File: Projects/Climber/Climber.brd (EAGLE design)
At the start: 160 x 100 mm, 3 parts, among them M1 VNH5019, M2 D36V6FX, U1 NRF52840-DONGLE

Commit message: New devices in Climber
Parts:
- added R1, R2: (no value), resistor:R0603
- added U$10: NET_CONN, NET_CONN:NET_CONN
- added U2: BSS138BKW, BSS138:SOT65P210X110-3N
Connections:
- net VOUT renamed M1_VOUT
- new net M1_CS: M1.CS
- new net M1_ENA/DIAGA: M1.ENA
- new net M1_ENB/DIAGB: M1.ENB
- new net M1_INA: M1.INA
- new net M1_INB: M1.INB
- new net M1_PWM: M1.PWM
- new net NEO_HV: R2.1, U2.3
- new net NEO_LV: R1.1, U2.2
- new net VDD_5V: R2.2
- net GND: now also U$10.1, U$10.2
- net VDD: now also M2.VOUT, R1.2, U1.OUT
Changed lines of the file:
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@@
 <layer number="111" name="LPC17xx" color="7" fill="1" visible="yes" active="yes"/>
 <layer number="112" name="tSilk" color="7" fill="1" visible="yes" active="yes"/>
+<layer number="113" name="FRNTTEKEN" color="7" fill="1" visible="yes" active="yes"/>
+<layer number="114" name="FRNTMAAT1" color="7" fill="1" visible="yes" active="yes"/>
+<layer number="115" name="FRNTMAAT2" color="7" fill="1" visible="yes" active="yes"/>
 <layer number="116" name="Patch_BOT" color="9" fill="4" visible="yes" active="yes"/>
+<layer number="117" name="BACKMAAT1" color="7" fill="1" visible="yes" active="yes"/>
+<layer number="118" name="BACKMAAT2" color="7" fill="1" visible="yes" active="yes"/>
+<layer number="119" name="KAP_TEKEN" color="7" fill="1" visible="yes" active="yes"/>
 <layer number="120" name="_Dimension" color="7" fill="1" visible="yes" active="yes"/>
 <layer number="121" name="_tsilk" color="6" fill="1" visible="yes" active="yes"/>
@@
 <layer number="127" name="_tValues" color="6" fill="1" visible="yes" active="yes"/>
 <layer number="128" name="_bValues" color="6" fill="1" visible="yes" active="yes"/>
+<layer number="130" name="SMDSTROOK" color="7" fill="1" visible="yes" active="yes"/>
 <layer number="131" name="tAdjust" color="7" fill="1" visible="yes" active="yes"/>
 <layer number="132" name="bAdjust" color="7" fill="1" visible="yes" active="yes"/>
@@
 <layer number="251" name="bxdocu" color="7" fill="1" visible="no" active="yes"/>
 <layer number="254" name="cooling" color="7" fill="1" visible="yes" active="yes"/>
+<layer number="255" name="Accent" color="7" fill="1" visible="yes" active="yes"/>
 </layers>
 <board>
@@
 <attribute name="VALUE" x="30.9626" y="59.69" size="1.27" layer="27" rot="R180"/>
 </element>
+<element name="U2" library="BSS138" package="SOT65P210X110-3N" value="BSS138BKW" x="-17.78" y="2.54" smashed="yes">
+<attribute name="MPN" value="BSS138BKW" x="-17.78" y="2.54" size="1.778" layer="27" display="off"/>
+<attribute name="NAME" x="-18.3642" y="3.8196" size="0.254" layer="25" ratio="10" rot="SR0"/>
+<attribute name="OC_FARNELL" value="2053836" x="-17.78" y="2.54" size="1.778" layer="27" display="off"/>
+<attribute name="OC_NEWARK" value="61T7488" x="-17.78" y="2.54" size="1.778" layer="27" display="off"/>
+<attribute name="PACKAGE" value="SOT-23-3" x="-17.78" y="2.54" size="1.778" layer="27" display="off"/>
+<attribute name="SUPPLIER" value="NXP" x="-17.78" y="2.54" size="1.778" layer="27" display="off"/>
+<attribute name="VALUE" x="-18.3642" y="1.043" size="0.254" layer="27" ratio="10" rot="SR0"/>
+</element>
+<element name="U$10" library="NET_CONN" package="NET_CONN" value="NET_CONN" x="-19.05" y="-1.27" smashed="yes"/>
+<element name="R1" library="resistor" package="R0603" value="" x="-17.78" y="-5.08" smashed="yes">
+<attribute name="NAME" x="-17.526" y="-3.937" size="0.381" layer="25" rot="R180"/>
+<attribute name="VALUE" x="-19.304" y="-6.223" size="0.381" layer="27"/>
+</element>
+<element name="R2" library="resistor" package="R0603" value="" x="-17.78" y="-8.89" smashed="yes">
+<attribute name="NAME" x="-17.526" y="-7.747" size="0.381" layer="25" rot="R180"/>
+<attribute name="VALUE" x="-19.304" y="-10.033" size="0.381" layer="27"/>
+</element>
 </elements>
 <signals>
 <signal name="VDD">
 <contactref element="M1" pad="VDD"/>
+<contactref element="M2" pad="VOUT"/>
+<contactref element="U1" pad="OUT"/>
+<contactref element="R1" pad="2"/>
+<wire x1="44.45" y1="83.82" x2="57.15" y2="86.36" width="0" layer="19" extent="1-1"/>
+<wire x1="5.0876" y1="57.15" x2="44.45" y2="83.82" width="0" layer="19" extent="1-1"/>
+<wire x1="-16.93" y1="-5.08" x2="5.0876" y2="57.15" width="0" layer="19" extent="1-1"/>
 </signal>
 <signal name="GND">
 <contactref element="M1" pad="GND@0"/>
 <contactref element="M1" pad="GND@1"/>
+<contactref element="U1" pad="G3"/>
+<contactref element="U1" pad="G1"/>
+<contactref element="U1" pad="G2"/>
+<contactref element="U$10" pad="1"/>
+<contactref element="U$10" pad="2"/>
 <contactref element="M2" pad="GND"/>
-<contactref element="U1" pad="G1"/>
-<contactref element="U1" pad="G3"/>
-<contactref element="U1" pad="G2"/>
 <wire x1="44.45" y1="86.36" x2="59.69" y2="86.36" width="0" layer="19" extent="1-1"/>
 <wire x1="44.45" y1="91.44" x2="44.45" y2="86.36" width="0" layer="19" extent="1-1"/>
-<wire x1="25.4076" y1="41.91" x2="44.45" y2="86.36" width="0" layer="19" extent="1-1"/>
-<wire x1="25.4076" y1="57.15" x2="25.4076" y2="41.91" width="0" layer="19" extent="1-1"/>
+<wire x1="25.4076" y1="57.15" x2="44.45" y2="86.36" width="0" layer="19" extent="1-1"/>
+<wire x1="25.4076" y1="41.91" x2="25.4076" y2="57.15" width="0" layer="19" extent="1-1"/>
 <wire x1="7.6276" y1="57.15" x2="25.4076" y2="57.15" width="0" layer="19" extent="1-1"/>
-</signal>
-<signal name="VOUT">
-<contactref element="M1" pad="VOUT"/>
+<wire x1="-17.55" y1="-1.27" x2="25.4076" y2="41.91" width="0" layer="19" extent="1-1"/>
+<wire x1="-18.669" y1="-1.27" x2="-17.55" y2="-1.27" width="0" layer="19" extent="1-1"/>
 </signal>
 <signal name="VIN">
@@
 <contactref element="U1" pad="VBUS"/>
 </signal>
+<signal name="NEO_LV">
+<contactref element="R1" pad="1"/>
+<contactref element="U2" pad="2"/>
+<wire x1="-18.7198" y1="1.8796" x2="-18.63" y2="-5.08" width="0" layer="19" extent="1-1"/>
+</signal>
+<signal name="NEO_HV">
+<contactref element="U2" pad="3"/>
+<contactref element="R2" pad="1"/>
+<wire x1="-16.8402" y1="2.54" x2="-18.63" y2="-8.89" width="0" layer="19" extent="1-1"/>
+</signal>
+<signal name="VDD_5V">
+<contactref element="R2" pad="2"/>
+</signal>
+<signal name="M1_INA">
+<contactref element="M1" pad="INA"/>
+</signal>
+<signal name="M1_INB">
+<contactref element="M1" pad="INB"/>
+</signal>
+<signal name="M1_ENA/DIAGA">
+<contactref element="M1" pad="ENA"/>
+</signal>
+<signal name="M1_ENB/DIAGB">
+<contactref element="M1" pad="ENB"/>
+</signal>
+<signal name="M1_PWM">
+<contactref element="M1" pad="PWM"/>
+</signal>
+<signal name="M1_VOUT">
+<contactref element="M1" pad="VOUT"/>
+</signal>
+<signal name="M1_CS">
+<contactref element="M1" pad="CS"/>
+</signal>
 </signals>

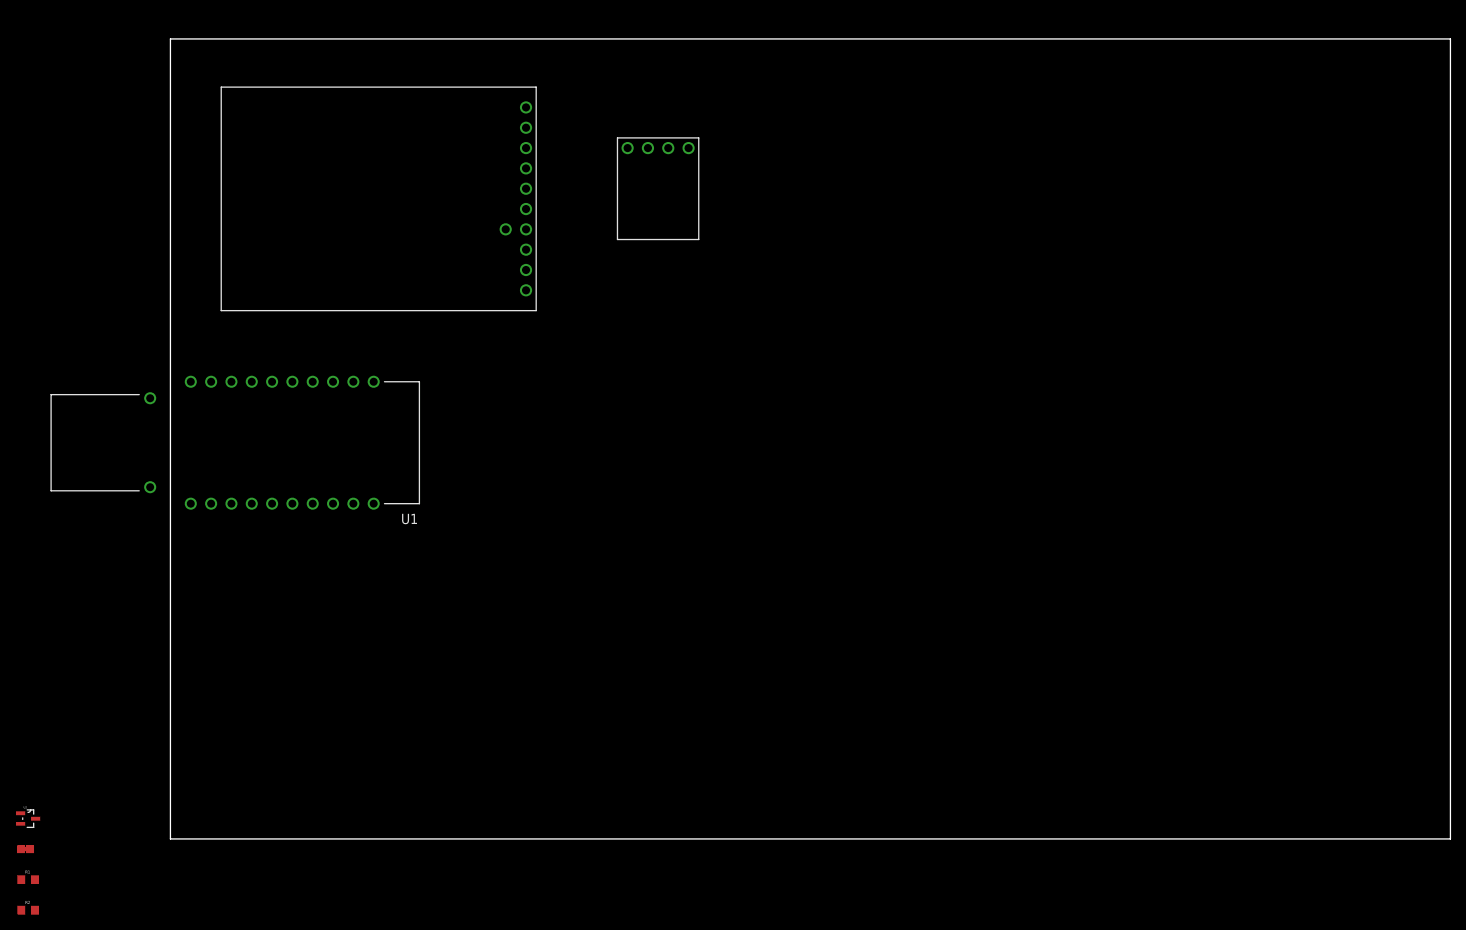
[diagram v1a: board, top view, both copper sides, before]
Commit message: Added ZLL PCB, finished climber PCB
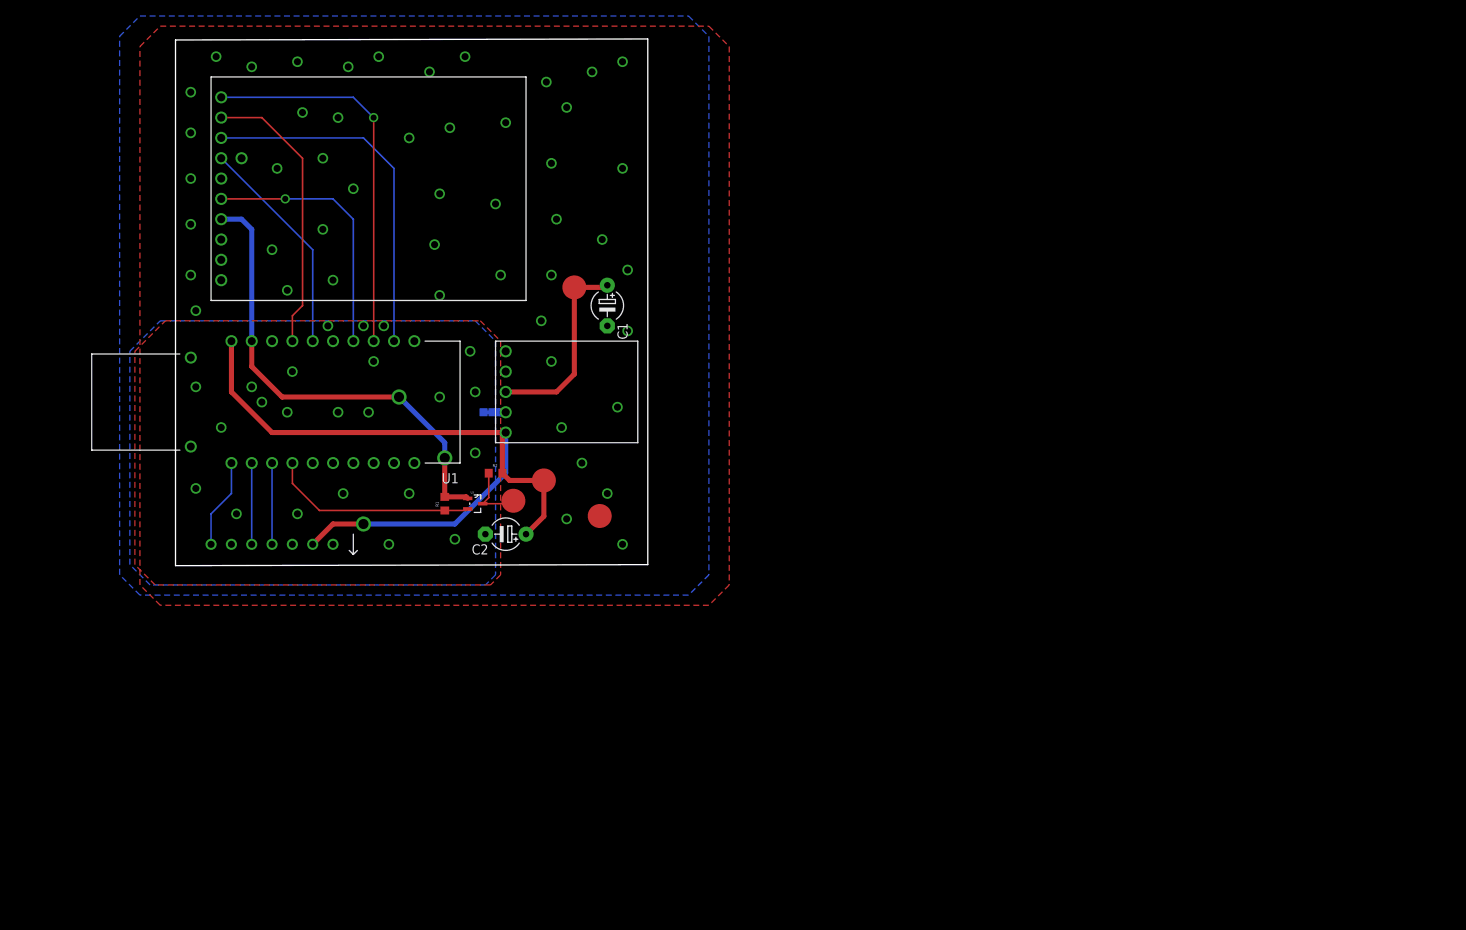
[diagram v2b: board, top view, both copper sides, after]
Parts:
- added 5V, NEO, NEO1, VIN: PAD3MM, Exposed_pad:PAD_3
- added C1, C2: (no value), resistor:E5-4
- added U$13: VL53L1X, Pololu:VL53L1X
- M2: value D36V6FX -> D24V10FX; device Pololu:D36V6FX -> Pololu:D24V10FX
- R1, R2: value (none) -> 10k
- moved U$10 80.9 mm to (40.6, 53.3), flipped to the bottom
- moved R2 80.0 mm to (40.6, 45.7)
- moved R1 70.1 mm to (34.3, 41.9), turned to 90 degrees
- moved U2 68.4 mm to (38.1, 41.9)
- moved M1 43.8 mm to (6.35, 69.8), turned to 90 degrees
- moved M2 38.7 mm to (41.9, 50.8), turned to 90 degrees
- moved U1 7.18 mm to (30.5, 47.0)
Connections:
- net M1_VOUT renamed VOUT
- removed net M1_ENB/DIAGB: M1.ENB
- removed net VBUS: U1.VBUS
- removed net VIN: M2.VIN
- new net 12V: C1.+, M2.VIN, VIN.P$1
- new net GPIO1: U$13.GPIO1, U1.0.13
- new net NC: U$13.VDD
- new net PWR_GND: C1.-, M1.GND@0, M1.GND@1, M2.GND, NEO1.P$1, U$10.1
- new net SCL: U$13.SCL, U1.0.15
- new net SDA: U$13.SDA, U1.0.17
- net GND: now also C2.-, U$13.GND; no longer M1.GND@0, M1.GND@1, M2.GND, U$10.1
- net M1_CS: now also U1.0.29
- net M1_ENA/DIAGA: now also U1.0.31
- net M1_INA: now also U1.1.13
- net M1_INB: now also U1.1.15
- net M1_PWM: now also U1.1.10
- net NEO_HV: now also NEO.P$1
- net NEO_LV: now also U1.0.20
- net VDD: now also U2.1; no longer M2.VOUT
- net VDD_5V: now also 5V.P$1, C2.+, M2.VOUT, U$13.VIN, U1.VBUS
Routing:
- net VDD_5V: track 0.00 -> 94.1 mm, vias 0 -> 1
- net VDD: track 0.00 -> 59.3 mm, vias 0 -> 2
- net M1_INA: track 0.00 -> 48.0 mm, vias 0 -> 1
- net M1_PWM: track 0.00 -> 44.8 mm
- net M1_ENA/DIAGA: track 0.00 -> 35.7 mm
- net M1_INB: track 0.00 -> 32.8 mm, vias 0 -> 1
- net M1_CS: track 0.00 -> 27.6 mm
- net NEO_LV: track 0.00 -> 25.9 mm
- net 12V: track 0.00 -> 24.6 mm
- net GPIO1: track 0.00 -> 11.2 mm
- net SDA: track 0.00 -> 10.2 mm
- net SCL: track 0.00 -> 10.2 mm
- net NEO_HV: track 0.00 -> 8.10 mm
- net PWR_GND: track 0.00 -> 2.67 mm, vias 0 -> 49
- added copper zone on layer 1, net GND
- added copper zone on layer 16, net GND
- added copper zone on layer 1, net PWR_GND
- added copper zone on layer 16, net PWR_GND
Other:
- board size 160 x 100 mm -> 59 x 65.8 mm

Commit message: Updated stravaV3 Updated Climber
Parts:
- moved M2 31.8 mm to (57.1, 78.7), turned to 180 degrees
- moved NEO1 28.8 mm to (56.5, 67.9)
- moved U1 27.9 mm to (58.4, 46.4)
- moved U$10 19.8 mm to (55.2, 66.7), turned to 270 degrees
- moved 5V 16.2 mm to (31.8, 36.8)
- moved R1 12.7 mm to (47.0, 41.9), turned to 270 degrees
- moved R2 12.1 mm to (48.9, 36.8), turned to 270 degrees
- moved C2 11.5 mm to (53.3, 39.4), turned to 90 degrees
- moved U2 8.84 mm to (46.4, 38.7), turned to 270 degrees
- moved C1 8.35 mm to (53.3, 74.9), turned to 0 degrees
- moved NEO 3.17 mm to (42.5, 38.1)
- moved VIN 2.54 mm to (50.2, 70.5)
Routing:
- net M1_CS: track 27.6 -> 55.0 mm, vias 0 -> 2
- net GPIO1: track 11.2 -> 37.4 mm
- net M1_ENA/DIAGA: track 35.7 -> 59.4 mm, vias 0 -> 2
- net SCL: track 10.2 -> 33.7 mm
- net SDA: track 10.2 -> 33.7 mm
- net M1_INB: track 32.8 -> 52.5 mm, vias 1 -> 0
- net M1_INA: track 48.0 -> 66.9 mm, vias 1 -> 2
- net M1_PWM: track 44.8 -> 63.1 mm
- net 12V: track 24.6 -> 7.91 mm
- net NEO_LV: track 25.9 -> 10.6 mm
- net VDD: track 59.3 -> 69.9 mm, vias 2 -> 1
- net PWR_GND: track 2.67 -> 12.0 mm, vias 49 -> 41
- net VDD_5V: track 94.1 -> 100.4 mm
- net NEO_HV: track 8.10 -> 6.78 mm

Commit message: Order @ Boktech
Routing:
- net VDD_5V: track 100.4 -> 98.6 mm
- net GPIO1: track 37.4 -> 36.7 mm
- net M1_CS: track 55.0 -> 55.5 mm
- net PWR_GND: vias 41 -> 42
